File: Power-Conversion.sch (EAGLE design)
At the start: 49 parts, among them Q1 SUM90P10-19L, U7 LM2678

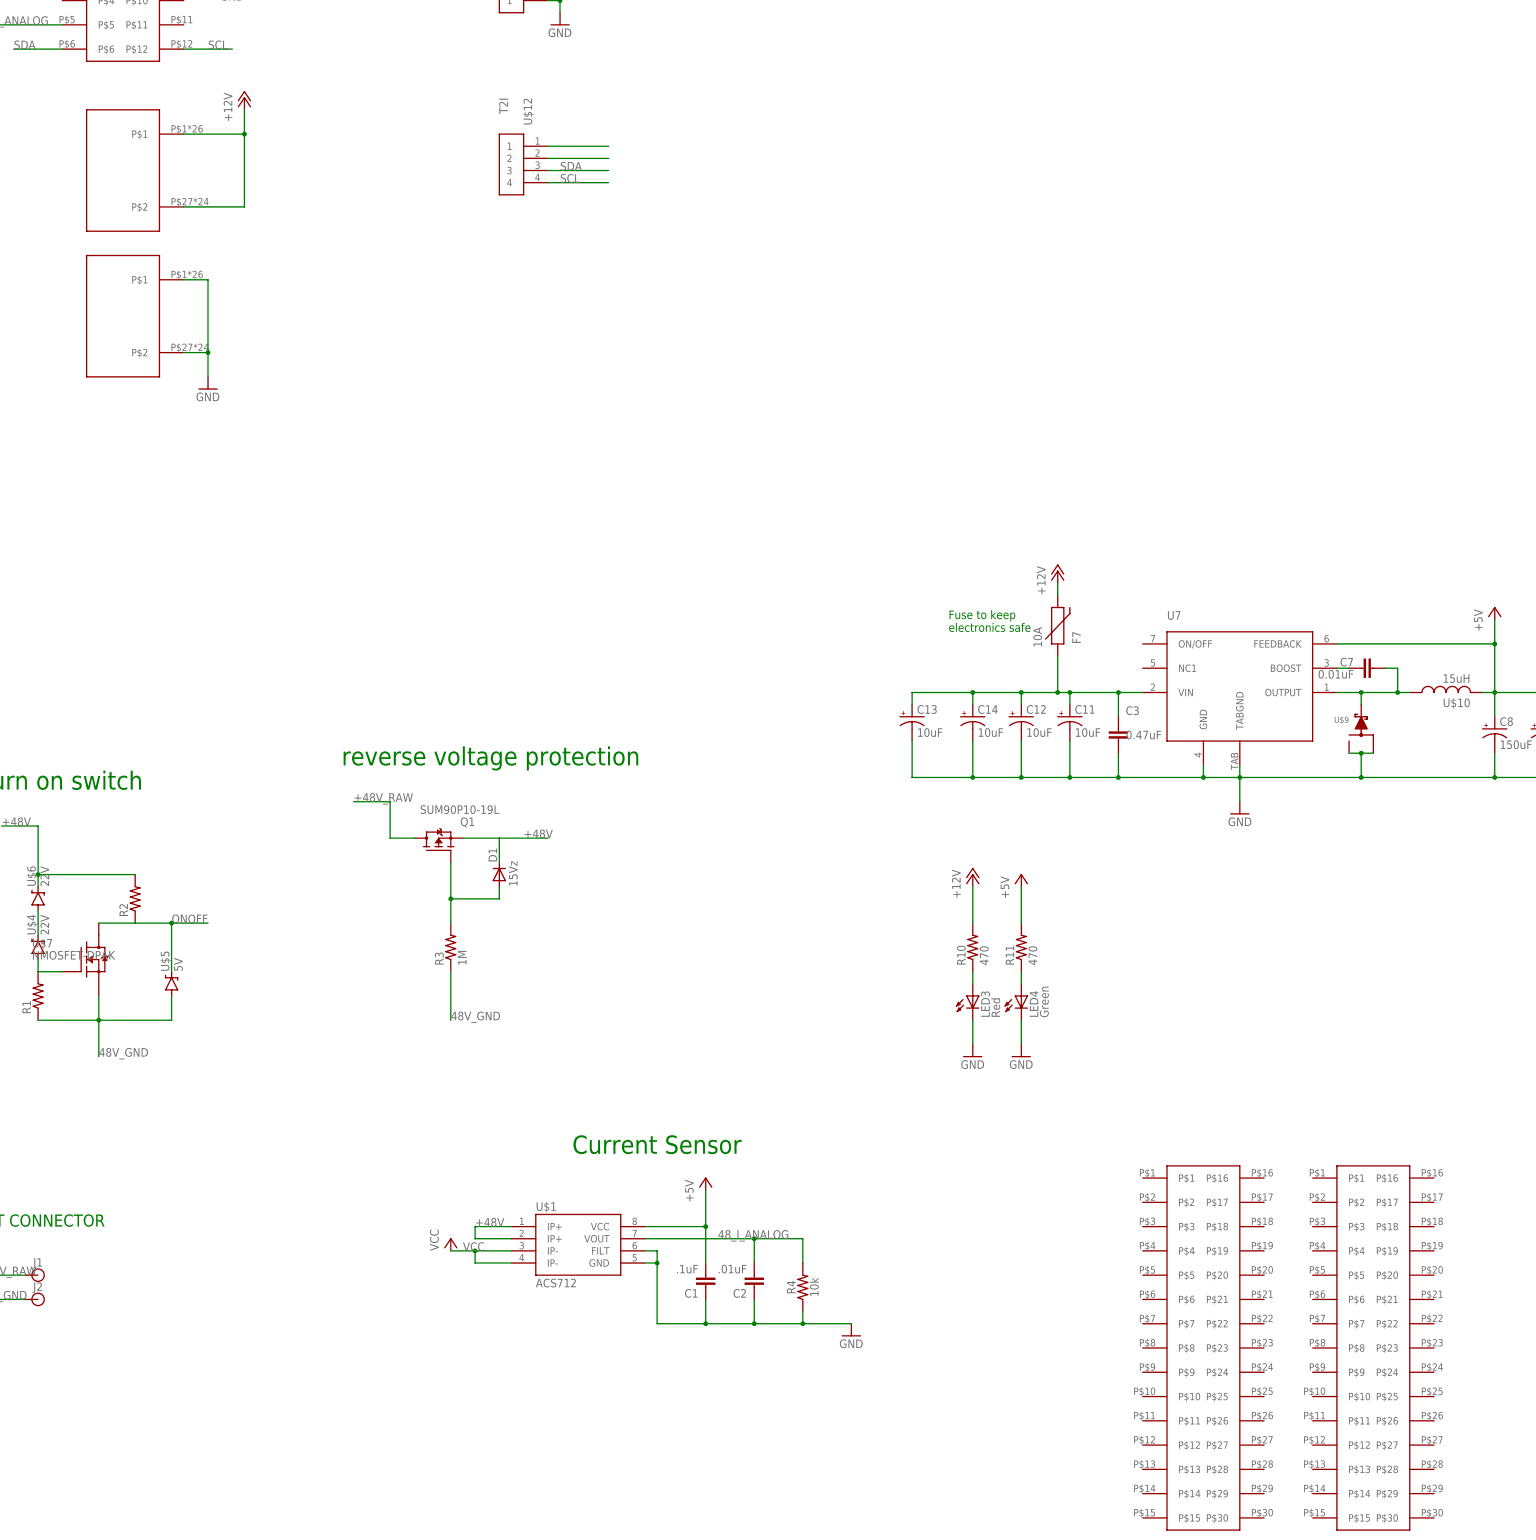
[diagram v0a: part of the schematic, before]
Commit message: Added standard ESC board connector
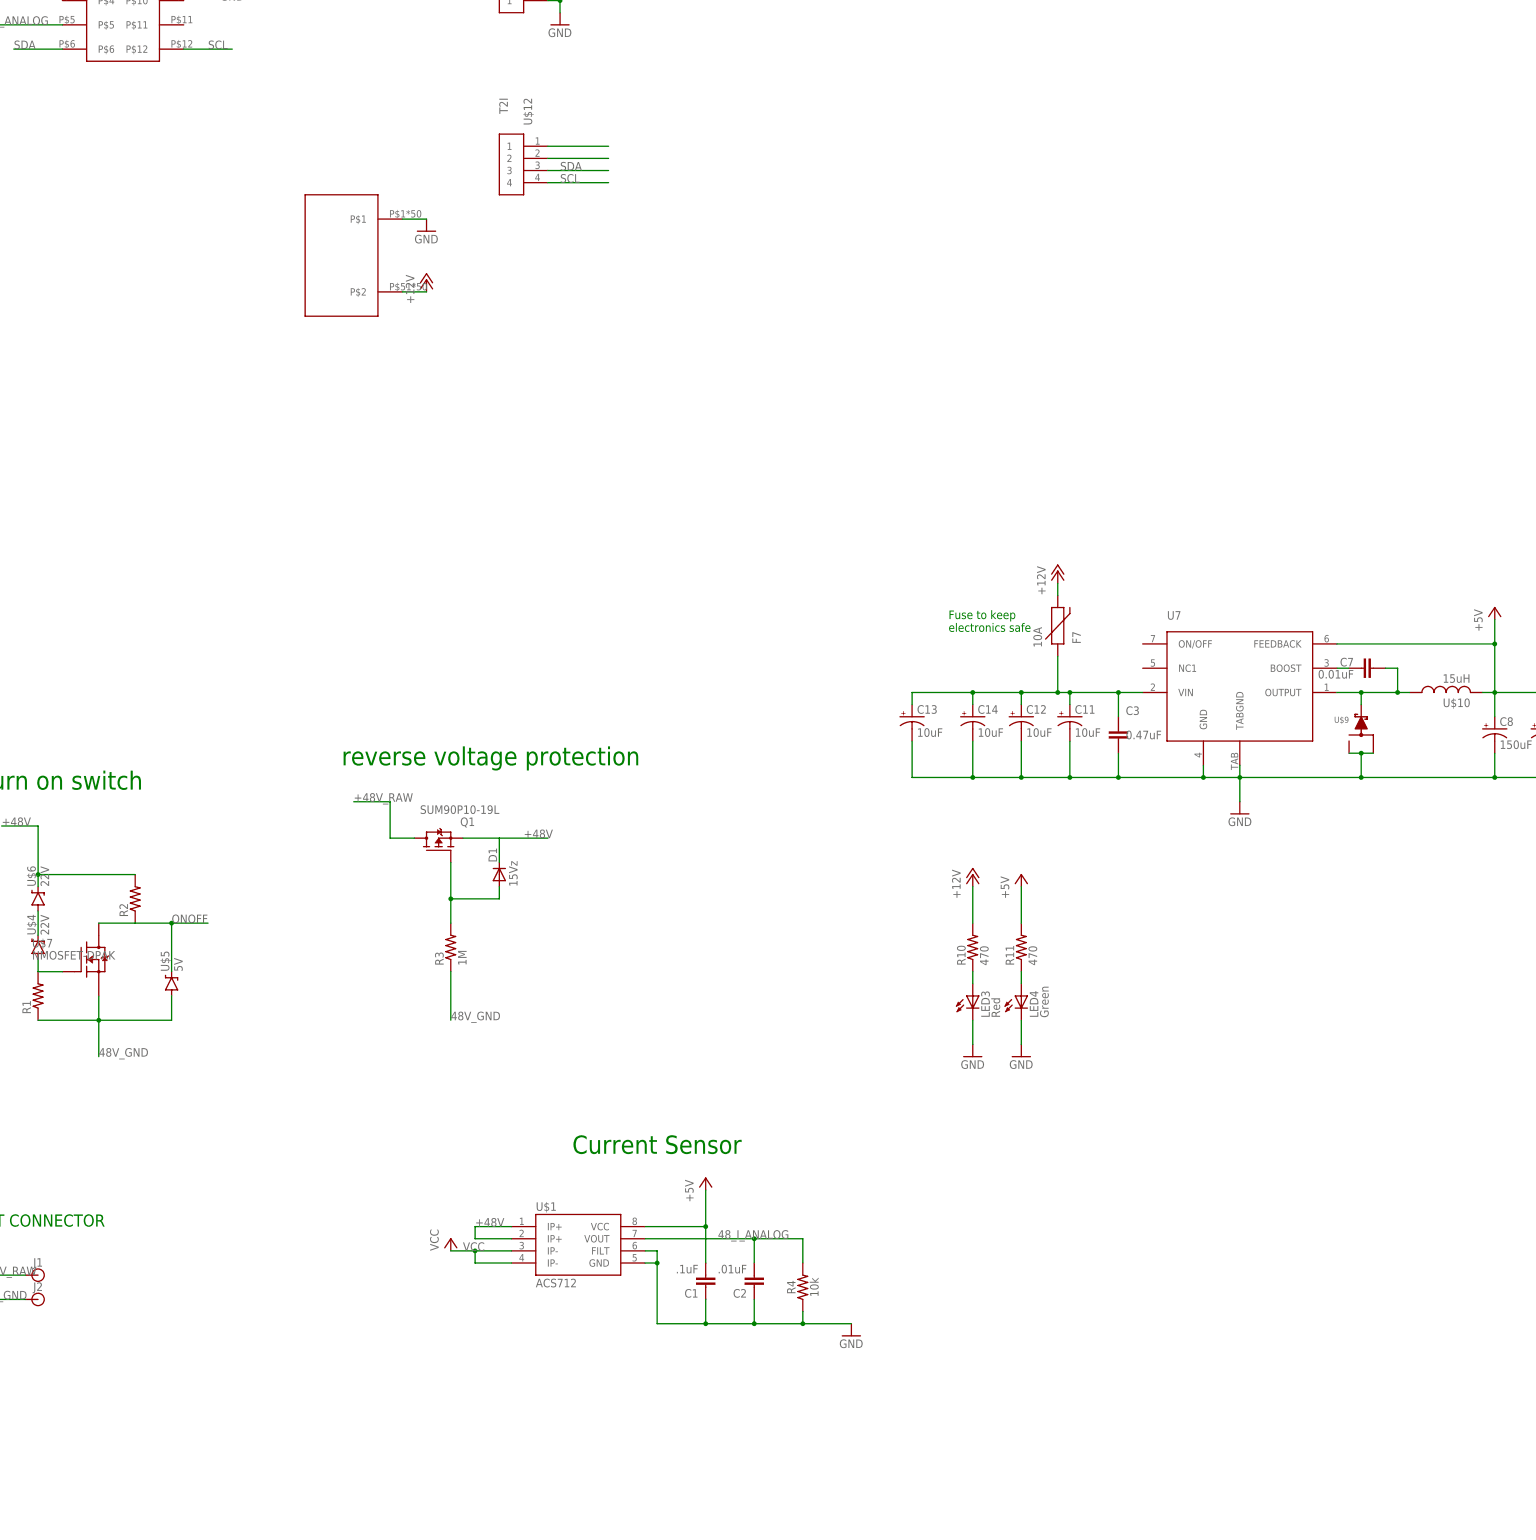
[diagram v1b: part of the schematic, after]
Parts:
- removed U$13, U$14: POWER_BRICK_CONNECTORS(2X15), MotherBoardParts2:POWER_BRICK_CONNECTORS(2X15)
- removed U$3, U$8: POWER-BRICK-CONNECTOR, MotherboardParts:POWER-BRICK-CONNECTOR
- added U$17: ESC-CONNECTORESC-CONNECTOR, MotherboardParts:ESC-CONNECTORESC-CONNECTOR
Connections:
- net +12V: now also U$17.P$2; no longer U$8.P$1, U$8.P$2
- net GND: now also U$17.P$1; no longer U$3.P$1, U$3.P$2
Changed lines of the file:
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@@
 <?xml version="1.0" encoding="utf-8"?>
 <!DOCTYPE eagle SYSTEM "eagle.dtd">
-<eagle version="8.4.3">
+<eagle version="8.5.0">
 <drawing>
 <settings>
@@
 <part name="J1" library="SparkFun-Connectors" deviceset="BANANA_CONN" device=""/>
 <part name="J2" library="SparkFun-Connectors" deviceset="BANANA_CONN" device=""/>
-<part name="U$3" library="MotherboardParts" deviceset="POWER-BRICK-CONNECTOR" device=""/>
-<part name="U$8" library="MotherboardParts" deviceset="POWER-BRICK-CONNECTOR" device=""/>
 <part name="U$16" library="MotherBoardParts2" deviceset="POWER_BRICK_CONNECTORS(2X6)" device=""/>
 <part name="GND6" library="supply1" deviceset="GND" device=""/>
@@
 <part name="GND7" library="supply1" deviceset="GND" device=""/>
 <part name="P+16" library="supply1" deviceset="+5V" device=""/>
-<part name="U$13" library="MotherBoardParts2" deviceset="POWER_BRICK_CONNECTORS(2X15)" device=""/>
-<part name="U$14" library="MotherBoardParts2" deviceset="POWER_BRICK_CONNECTORS(2X15)" device=""/>
 <part name="P+17" library="supply1" library_urn="urn:adsk.eagle:library:371" deviceset="VCC" device=""/>
 <part name="F7" library="PowerComponents" deviceset="PTC(2920L)" device="" value="10A"/>
 <part name="P+18" library="supply1" deviceset="+12V" device=""/>
+<part name="U$17" library="MotherboardParts" deviceset="ESC-CONNECTOR" device="ESC-CONNECTOR"/>
 </parts>
 <sheets>
@@
 <instance part="J1" gate="G$1" x="33.02" y="104.14"/>
 <instance part="J2" gate="G$1" x="33.02" y="99.06"/>
-<instance part="U$3" gate="G$1" x="50.8" y="304.8"/>
-<instance part="U$8" gate="G$1" x="50.8" y="335.28"/>
 <instance part="U$16" gate="G$1" x="50.8" y="378.46"/>
 <instance part="GND6" gate="1" x="73.66" y="373.38"/>
@@
 <instance part="U$18" gate="G$1" x="142.24" y="441.96"/>
 <instance part="U$19" gate="G$1" x="233.68" y="441.96"/>
-<instance part="GND5" gate="1" x="68.58" y="289.56"/>
+<instance part="GND5" gate="1" x="114.3" y="322.58"/>
 <instance part="U$20" gate="G$1" x="50.8" y="482.6"/>
 <instance part="U$21" gate="G$1" x="139.7" y="482.6"/>
@@
 <instance part="P+13" gate="1" x="320.04" y="462.28"/>
 <instance part="P+14" gate="1" x="27.94" y="388.62"/>
-<instance part="P+15" gate="1" x="76.2" y="350.52"/>
+<instance part="P+15" gate="1" x="114.3" y="312.42"/>
 <instance part="R15" gate="G$1" x="187.96" y="520.7" rot="R180"/>
 <instance part="R5" gate="G$1" x="187.96" y="510.54" rot="R180"/>
@@
 <instance part="GND7" gate="1" x="142.24" y="365.76"/>
 <instance part="P+16" gate="1" x="142.24" y="388.62"/>
-<instance part="U$13" gate="G$1" x="276.86" y="91.44"/>
-<instance part="U$14" gate="G$1" x="312.42" y="91.44"/>
 <instance part="P+17" gate="VCC" x="119.38" y="111.76"/>
 <instance part="F7" gate="G$1" x="246.38" y="238.76" rot="MR90"/>
 <instance part="P+18" gate="1" x="246.38" y="251.46"/>
+<instance part="U$17" gate="G$1" x="96.52" y="317.5"/>
 </instances>
 <busses>
@@
 </segment>
 <segment>
-<pinref part="U$3" gate="G$1" pin="P$2"/>
-<wire x1="63.5" y1="297.18" x2="68.58" y2="297.18" width="0.1524" layer="91"/>
-<wire x1="68.58" y1="297.18" x2="68.58" y2="292.1" width="0.1524" layer="91"/>
-<pinref part="GND5" gate="1" pin="GND"/>
-<pinref part="U$3" gate="G$1" pin="P$1"/>
-<wire x1="63.5" y1="312.42" x2="68.58" y2="312.42" width="0.1524" layer="91"/>
-<wire x1="68.58" y1="312.42" x2="68.58" y2="297.18" width="0.1524" layer="91"/>
-<junction x="68.58" y="297.18"/>
-</segment>
-<segment>
 <pinref part="U$20" gate="G$1" pin="D_GND"/>
 <wire x1="68.58" y1="472.44" x2="73.66" y2="472.44" width="0.1524" layer="91"/>
@@
 <wire x1="139.7" y1="370.84" x2="142.24" y2="370.84" width="0.1524" layer="91"/>
 <junction x="142.24" y="370.84"/>
+</segment>
+<segment>
+<pinref part="U$17" gate="G$1" pin="P$1"/>
+<wire x1="109.22" y1="325.12" x2="114.3" y2="325.12" width="0.1524" layer="91"/>
+<pinref part="GND5" gate="1" pin="GND"/>
 </segment>
 </net>
@@
 </segment>
 <segment>
-<pinref part="U$8" gate="G$1" pin="P$1"/>
-<wire x1="63.5" y1="342.9" x2="76.2" y2="342.9" width="0.1524" layer="91"/>
-<wire x1="76.2" y1="342.9" x2="76.2" y2="347.98" width="0.1524" layer="91"/>
-<pinref part="U$8" gate="G$1" pin="P$2"/>
-<wire x1="63.5" y1="327.66" x2="76.2" y2="327.66" width="0.1524" layer="91"/>
-<wire x1="76.2" y1="327.66" x2="76.2" y2="342.9" width="0.1524" layer="91"/>
-<junction x="76.2" y="342.9"/>
-<pinref part="P+15" gate="1" pin="+12V"/>
-</segment>
-<segment>
 <pinref part="F7" gate="G$1" pin="2"/>
 <pinref part="P+18" gate="1" pin="+12V"/>
 <wire x1="246.38" y1="246.38" x2="246.38" y2="248.92" width="0.1524" layer="91"/>
 </segment>
-</net>
+<segment>
+<pinref part="U$17" gate="G$1" pin="P$2"/>
+<wire x1="109.22" y1="309.88" x2="114.3" y2="309.88" width="0.1524" layer="91"/>
+<pinref part="P+15" gate="1" pin="+12V"/>
+</segment>
+</net>

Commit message: Some routing done
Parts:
- U$17: value ESC-CONNECTORESC-CONNECTOR -> ESC-CONNECTORPARALLELL; device MotherboardParts:ESC-CONNECTORESC-CONNECTOR -> MotherboardParts:ESC-CONNECTORPARALLELL
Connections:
- removed net SCL4: U$23.SCL
- removed net SDA4: U$23.SDA
- net SCL1: now also U$23.SCL
- net SDA1: now also U$23.SDA
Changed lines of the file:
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@@
 <layer number="18" name="Vias" color="2" fill="1" visible="no" active="no"/>
 <layer number="19" name="Unrouted" color="6" fill="1" visible="no" active="no"/>
-<layer number="20" name="Dimension" color="15" fill="1" visible="no" active="no"/>
+<layer number="20" name="Dimension" color="24" fill="1" visible="no" active="no"/>
 <layer number="21" name="tPlace" color="7" fill="1" visible="no" active="no"/>
 <layer number="22" name="bPlace" color="7" fill="1" visible="no" active="no"/>
@@
 <part name="F7" library="PowerComponents" deviceset="PTC(2920L)" device="" value="10A"/>
 <part name="P+18" library="supply1" deviceset="+12V" device=""/>
-<part name="U$17" library="MotherboardParts" deviceset="ESC-CONNECTOR" device="ESC-CONNECTOR"/>
+<part name="U$17" library="MotherboardParts" deviceset="ESC-CONNECTOR" device="PARALLELL" value="ESC-CONNECTORPARALLELL"/>
 </parts>
 <sheets>
@@
 <label x="193.04" y="520.7" size="1.778" layer="95"/>
 </segment>
+<segment>
+<pinref part="U$23" gate="G$1" pin="SDA"/>
+<wire x1="304.8" y1="477.52" x2="299.72" y2="477.52" width="0.1524" layer="91"/>
+</segment>
 </net>
 <net name="SCL1" class="0">
@@
 <label x="193.04" y="510.54" size="1.778" layer="95"/>
 </segment>
-</net>
-<net name="SDA4" class="0">
-<segment>
-<pinref part="U$23" gate="G$1" pin="SDA"/>
-<wire x1="304.8" y1="477.52" x2="299.72" y2="477.52" width="0.1524" layer="91"/>
-</segment>
-</net>
-<net name="SCL4" class="0">
 <segment>
 <pinref part="U$23" gate="G$1" pin="SCL"/>

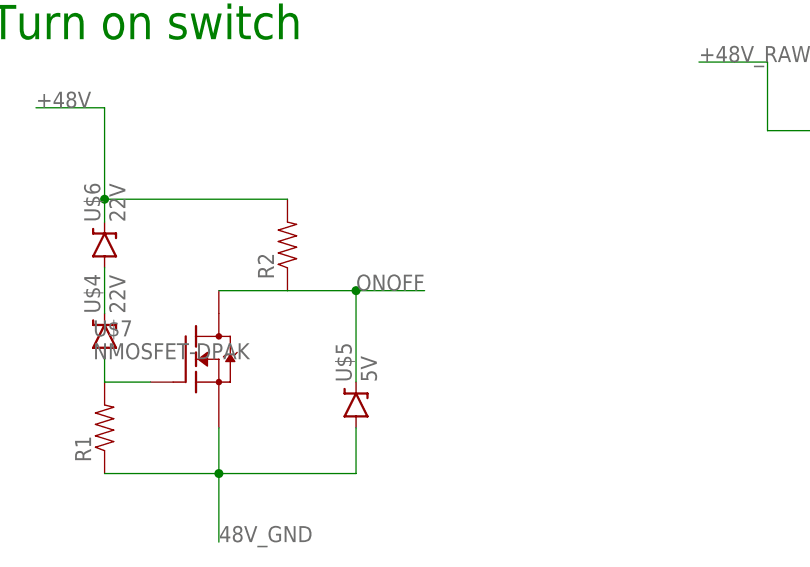
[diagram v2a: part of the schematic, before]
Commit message: finished board layout
first draft board layout
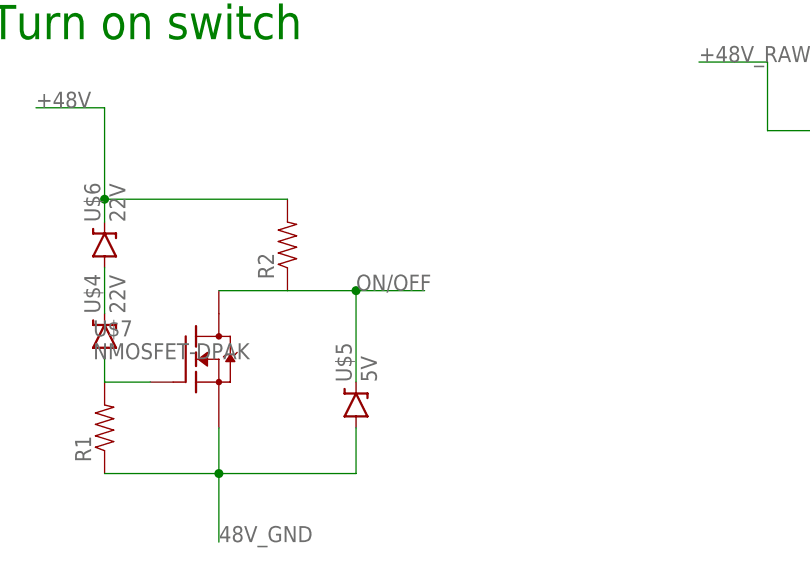
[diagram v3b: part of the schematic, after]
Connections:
- removed net ONOFF: R2.1, U$5.C, U$7.D1
- removed net V-: U$20.48V_GND, U$21.48V_GND, U$22.48V_GND, U$23.48V_GND
- net 48V_GND: now also U$20.48V_GND, U$21.48V_GND, U$22.48V_GND, U$23.48V_GND
- net ON/OFF: now also R2.1, U$5.C, U$7.D1
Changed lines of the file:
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@@
 <?xml version="1.0" encoding="utf-8"?>
 <!DOCTYPE eagle SYSTEM "eagle.dtd">
-<eagle version="8.5.0">
+<eagle version="8.3.2">
 <drawing>
 <settings>
@@
 </segment>
 </net>
-<net name="ONOFF" class="0">
-<segment>
-<pinref part="U$7" gate="G$1" pin="D1"/>
-<pinref part="R2" gate="G$1" pin="1"/>
-<wire x1="45.72" y1="177.8" x2="53.34" y2="177.8" width="0.1524" layer="91"/>
-<wire x1="53.34" y1="177.8" x2="60.96" y2="177.8" width="0.1524" layer="91"/>
-<pinref part="U$5" gate="G$1" pin="C"/>
-<wire x1="60.96" y1="167.64" x2="60.96" y2="177.8" width="0.1524" layer="91"/>
-<label x="60.96" y="177.8" size="1.778" layer="95"/>
-<wire x1="60.96" y1="177.8" x2="68.58" y2="177.8" width="0.1524" layer="91"/>
-<junction x="60.96" y="177.8"/>
-</segment>
-</net>
 <net name="N$9" class="0">
 <segment>
@@
 <label x="20.32" y="99.06" size="1.778" layer="95"/>
 </segment>
+<segment>
+<pinref part="U$20" gate="G$1" pin="48V_GND"/>
+<wire x1="68.58" y1="492.76" x2="73.66" y2="492.76" width="0.1524" layer="91"/>
+<pinref part="P-7" gate="1" pin="V-"/>
+</segment>
+<segment>
+<pinref part="U$21" gate="G$1" pin="48V_GND"/>
+<wire x1="157.48" y1="492.76" x2="162.56" y2="492.76" width="0.1524" layer="91"/>
+<pinref part="P-8" gate="1" pin="V-"/>
+</segment>
+<segment>
+<pinref part="U$22" gate="G$1" pin="48V_GND"/>
+<wire x1="251.46" y1="492.76" x2="256.54" y2="492.76" width="0.1524" layer="91"/>
+<pinref part="P-9" gate="1" pin="V-"/>
+</segment>
+<segment>
+<pinref part="U$23" gate="G$1" pin="48V_GND"/>
+<wire x1="337.82" y1="492.76" x2="342.9" y2="492.76" width="0.1524" layer="91"/>
+<pinref part="P-10" gate="1" pin="V-"/>
+</segment>
 </net>
 <net name="+12V" class="0">
@@
 <wire x1="304.8" y1="472.44" x2="299.72" y2="472.44" width="0.1524" layer="91"/>
 </segment>
+<segment>
+<pinref part="U$7" gate="G$1" pin="D1"/>
+<pinref part="R2" gate="G$1" pin="1"/>
+<wire x1="45.72" y1="177.8" x2="53.34" y2="177.8" width="0.1524" layer="91"/>
+<wire x1="53.34" y1="177.8" x2="60.96" y2="177.8" width="0.1524" layer="91"/>
+<pinref part="U$5" gate="G$1" pin="C"/>
+<wire x1="60.96" y1="167.64" x2="60.96" y2="177.8" width="0.1524" layer="91"/>
+<label x="60.96" y="177.8" size="1.778" layer="95"/>
+<wire x1="60.96" y1="177.8" x2="68.58" y2="177.8" width="0.1524" layer="91"/>
+<junction x="60.96" y="177.8"/>
+</segment>
 </net>
 <net name="+12V_1" class="0">
@@
 </segment>
 </net>
-<net name="V-" class="0">
-<segment>
-<pinref part="U$20" gate="G$1" pin="48V_GND"/>
-<wire x1="68.58" y1="492.76" x2="73.66" y2="492.76" width="0.1524" layer="91"/>
-<pinref part="P-7" gate="1" pin="V-"/>
-</segment>
-<segment>
-<pinref part="U$21" gate="G$1" pin="48V_GND"/>
-<wire x1="157.48" y1="492.76" x2="162.56" y2="492.76" width="0.1524" layer="91"/>
-<pinref part="P-8" gate="1" pin="V-"/>
-</segment>
-<segment>
-<pinref part="U$22" gate="G$1" pin="48V_GND"/>
-<wire x1="251.46" y1="492.76" x2="256.54" y2="492.76" width="0.1524" layer="91"/>
-<pinref part="P-9" gate="1" pin="V-"/>
-</segment>
-<segment>
-<pinref part="U$23" gate="G$1" pin="48V_GND"/>
-<wire x1="337.82" y1="492.76" x2="342.9" y2="492.76" width="0.1524" layer="91"/>
-<pinref part="P-10" gate="1" pin="V-"/>
-</segment>
-</net>
